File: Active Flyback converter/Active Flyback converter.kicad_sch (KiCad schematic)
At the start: 4 parts, among them J1 Conn_01x01_Pin, J2 Conn_01x01_Pin, J3 Conn_01x01_Pin, J7 Conn_01x01_Pin

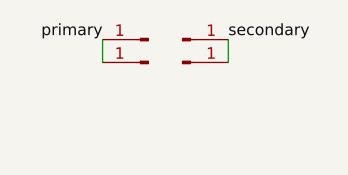
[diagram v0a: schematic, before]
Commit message: Active flyback converter - v1.2
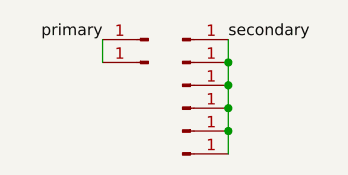
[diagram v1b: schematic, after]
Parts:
- added J4, J5, J6, J8: Conn_01x01_Pin, Connector_PinHeader_2.54mm:PinHeader_1x01_P2.54mm_Vertical, symbol Connector:Conn_01x01_Pin
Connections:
- net secondary: now also J4.1 (Pin_1), J5.1 (Pin_1), J6.1 (Pin_1), J8.1 (Pin_1)
